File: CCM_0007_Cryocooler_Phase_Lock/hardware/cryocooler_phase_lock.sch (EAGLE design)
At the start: 33 parts, among them Q1 CMA-4544PF-W, U1 MAX4466EXK+T, U3 PHOTON_WITH_HEADERS, X1 22-23-2021, X2 22-23-2021, X3 BNC_VERTICAL, X4 BNC_VERTICAL, X5 BNC_VERTICAL, X6 BNC_VERTICAL

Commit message: CCM_0007: finished initial board layout.
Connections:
- net N$11 renamed SYNC_OUT
- net N$13 renamed TRIGGER_OUT
- net N$8 renamed VOLUME_INDICATOR
- removed net N$7: R7.2, X3.SIGNAL
- new net N10: D1.C, R7.1, R8.2, U3.A1
- net DELAY_ADJUST: now also R7.2, X3.SIGNAL; no longer D1.C, R7.1, R8.2, U3.A1

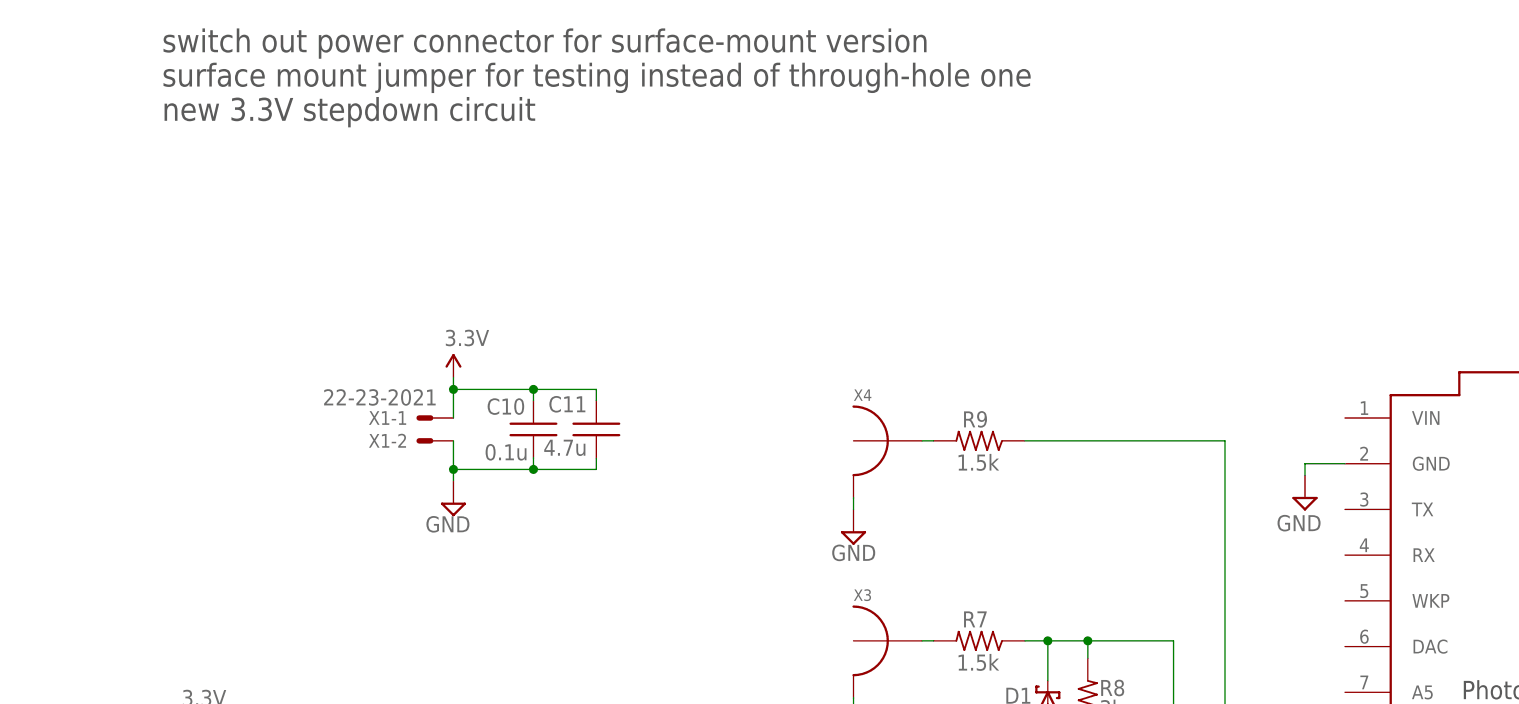
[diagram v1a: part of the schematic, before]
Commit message: More work on cryocooler interlock, uploaded ordering files.
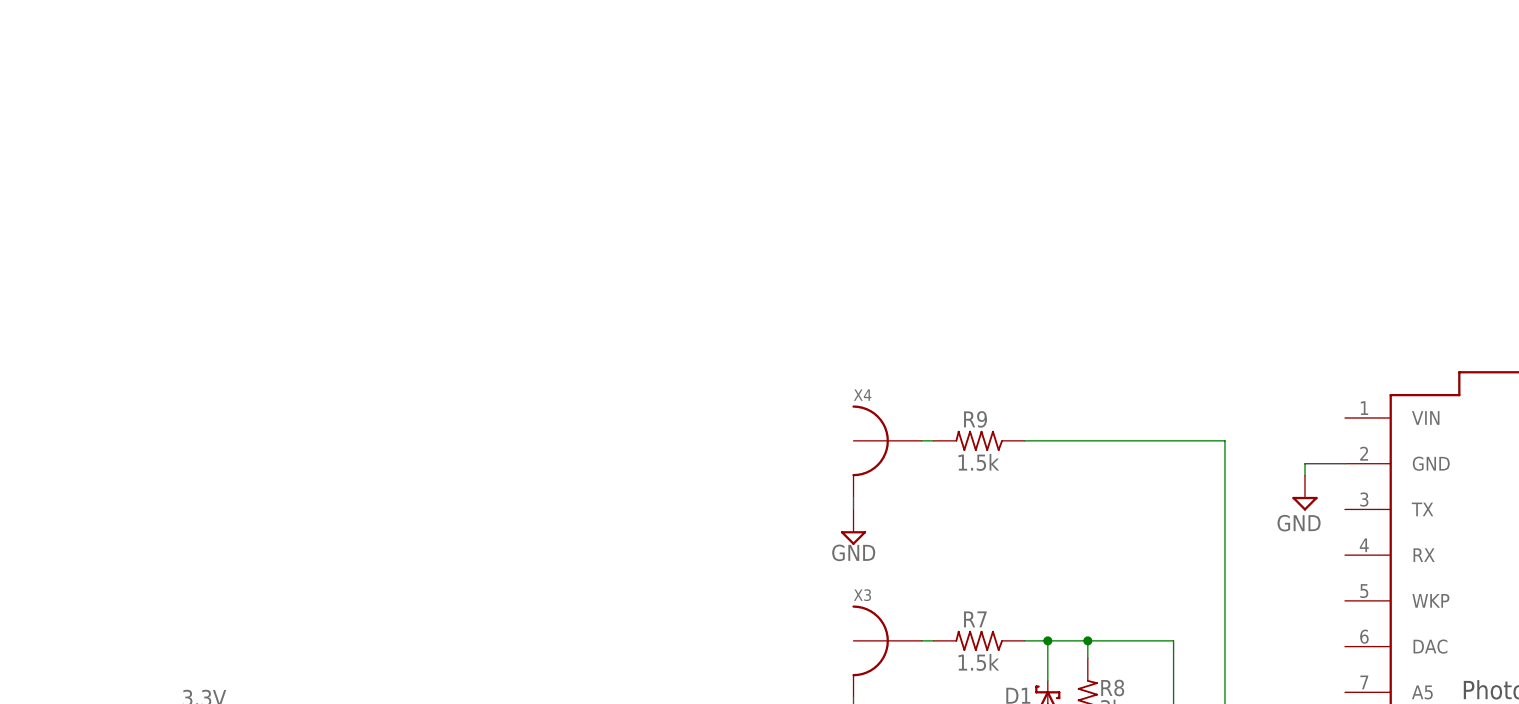
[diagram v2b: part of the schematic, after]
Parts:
- removed C10: 0.1u, acrooptics:C0603
- removed C11: 4.7u, acrooptics:C0805
- removed X1: 22-23-2021, con-molex:22-23-2021
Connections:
- net 3.3V: no longer C10.1, C11.2, X1-1.S
- net GND: no longer C10.2, C11.1, X1-2.S
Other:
- note added: "circuit powered from on-board Photon regulator which gets 5V from USB connection Plug into computer USB bus or use dedicated supply (e.g. Farnell 2451864)."
- note removed: "power input 3.3V at ~1A"
- note removed: "switch out power connector for surface-mount version surface mount jumper for testing instead of through-hole one new 3.3V stepdown circuit"
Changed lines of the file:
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@@
 <setting verticaltext="up"/>
 </settings>
-<grid distance="0.1" unitdist="inch" unit="inch" style="lines" multiple="1" display="no" altdistance="0.01" altunitdist="inch" altunit="inch"/>
+<grid distance="0.025" unitdist="inch" unit="inch" style="lines" multiple="1" display="no" altdistance="0.01" altunitdist="inch" altunit="inch"/>
 <layers>
 <layer number="1" name="Top" color="4" fill="1" visible="no" active="no"/>
@@
 <part name="C9" library="acrooptics" deviceset="C" device="0805" value="4.7u"/>
 <part name="SUPPLY5" library="supply2" deviceset="GND" device=""/>
-<part name="X1" library="con-molex" deviceset="22-23-2021" device=""/>
 <part name="P+1" library="SparkFun" deviceset="3.3V" device=""/>
-<part name="P+2" library="SparkFun" deviceset="3.3V" device=""/>
-<part name="SUPPLY1" library="supply2" deviceset="GND" device=""/>
 <part name="X2" library="con-molex" deviceset="22-23-2021" device=""/>
 <part name="P+3" library="SparkFun" deviceset="3.3V" device=""/>
@@
 <part name="SUPPLY10" library="supply2" deviceset="GND" device=""/>
 <part name="Q1" library="microbuilder" deviceset="ELECTRET" device="" value="CMA-4544PF-W"/>
-<part name="C10" library="acrooptics" deviceset="C" device="0603" value="0.1u"/>
-<part name="C11" library="acrooptics" deviceset="C" device="0805" value="4.7u"/>
 <part name="X4" library="noah" deviceset="BNC_VERTICAL" device=""/>
 <part name="X5" library="noah" deviceset="BNC_VERTICAL" device=""/>
@@
 <plain>
 <text x="-494.03" y="135.255" size="1.778" layer="97" rot="R180"></text>
-<text x="28.575" y="187.96" size="2.54" layer="97">switch out power connector for surface-mount version
-surface mount jumper for testing instead of through-hole one
-new 3.3V stepdown circuit</text>
 <text x="7.62" y="75.565" size="1.778" layer="150">From electret condenser microphone
 e.g. CMA-4544PF-W</text>
-<text x="36.83" y="151.13" size="1.778" layer="150">power input
-3.3V at ~1A</text>
 <text x="108.585" y="73.025" size="1.778" layer="150">optional high pass
 will block DC</text>
@@
 <text x="233.68" y="133.985" size="1.778" layer="150">sync out</text>
 <text x="234.95" y="112.395" size="1.778" layer="150">trigger out</text>
+<text x="138.43" y="160.655" size="1.778" layer="150">circuit powered from on-board Photon regulator
+which gets 5V from USB connection
+Plug into computer USB bus or use dedicated
+supply (e.g. Farnell 2451864).</text>
 </plain>
 <instances>
@@
 <attribute name="VALUE" x="152.4" y="144.145" size="1.778" layer="96" rot="MR180"/>
 </instance>
-<instance part="X1" gate="-1" x="58.42" y="154.94" rot="MR0"/>
-<instance part="X1" gate="-2" x="58.42" y="152.4" rot="MR0"/>
 <instance part="P+1" gate="G$1" x="212.09" y="156.21"/>
-<instance part="P+2" gate="G$1" x="60.96" y="159.385"/>
-<instance part="SUPPLY1" gate="GND" x="60.96" y="145.415" smashed="yes" rot="MR0">
-<attribute name="VALUE" x="62.865" y="142.24" size="1.778" layer="96" rot="MR0"/>
-</instance>
 <instance part="X2" gate="-1" x="29.21" y="101.6" rot="MR0"/>
 <instance part="X2" gate="-2" x="29.21" y="99.06" rot="MR0"/>
@@
 <attribute name="NAME" x="20.955" y="90.805" size="1.778" layer="95"/>
 <attribute name="VALUE" x="32.385" y="87.63" size="1.778" layer="96" rot="R180"/>
-</instance>
-<instance part="C10" gate="G$1" x="69.85" y="154.305" smashed="yes">
-<attribute name="NAME" x="68.961" y="157.099" size="1.778" layer="95" rot="R180"/>
-<attribute name="VALUE" x="64.389" y="150.241" size="1.778" layer="96"/>
-</instance>
-<instance part="C11" gate="G$1" x="76.835" y="153.035" smashed="yes" rot="MR180">
-<attribute name="NAME" x="75.819" y="155.575" size="1.778" layer="95" rot="MR0"/>
-<attribute name="VALUE" x="75.819" y="150.749" size="1.778" layer="96" rot="MR0"/>
 </instance>
 <instance part="X4" gate="G$1" x="105.41" y="152.4" smashed="yes">
@@
 <wire x1="160.02" y1="149.86" x2="155.575" y2="149.86" width="0.1524" layer="91"/>
 <wire x1="155.575" y1="149.86" x2="155.575" y2="148.59" width="0.1524" layer="91"/>
-</segment>
-<segment>
-<pinref part="X1" gate="-2" pin="S"/>
-<pinref part="SUPPLY1" gate="GND" pin="GND"/>
-<wire x1="60.96" y1="152.4" x2="60.96" y2="149.225" width="0.1524" layer="91"/>
-<pinref part="C10" gate="G$1" pin="2"/>
-<wire x1="60.96" y1="149.225" x2="60.96" y2="147.955" width="0.1524" layer="91"/>
-<wire x1="69.85" y1="150.495" x2="69.85" y2="149.225" width="0.1524" layer="91"/>
-<wire x1="69.85" y1="149.225" x2="60.96" y2="149.225" width="0.1524" layer="91"/>
-<junction x="60.96" y="149.225"/>
-<pinref part="C11" gate="G$1" pin="1"/>
-<wire x1="69.85" y1="149.225" x2="76.835" y2="149.225" width="0.1524" layer="91"/>
-<wire x1="76.835" y1="149.225" x2="76.835" y2="150.495" width="0.1524" layer="91"/>
-<junction x="69.85" y="149.225"/>
 </segment>
 <segment>
@@
 </segment>
 <segment>
-<pinref part="X1" gate="-1" pin="S"/>
-<pinref part="P+2" gate="G$1" pin="3.3V"/>
-<wire x1="60.96" y1="154.94" x2="60.96" y2="158.115" width="0.1524" layer="91"/>
-<pinref part="C10" gate="G$1" pin="1"/>
-<wire x1="60.96" y1="158.115" x2="60.96" y2="159.385" width="0.1524" layer="91"/>
-<wire x1="69.85" y1="156.845" x2="69.85" y2="158.115" width="0.1524" layer="91"/>
-<wire x1="69.85" y1="158.115" x2="60.96" y2="158.115" width="0.1524" layer="91"/>
-<junction x="60.96" y="158.115"/>
-<pinref part="C11" gate="G$1" pin="2"/>
-<wire x1="69.85" y1="158.115" x2="76.835" y2="158.115" width="0.1524" layer="91"/>
-<wire x1="76.835" y1="158.115" x2="76.835" y2="156.845" width="0.1524" layer="91"/>
-<junction x="69.85" y="158.115"/>
-</segment>
-<segment>
